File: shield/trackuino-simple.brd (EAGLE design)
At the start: 31.4 x 55.9 mm, 11 parts, among them T1 BC547, U1 ARDUINO_SHIELDNOHOLES

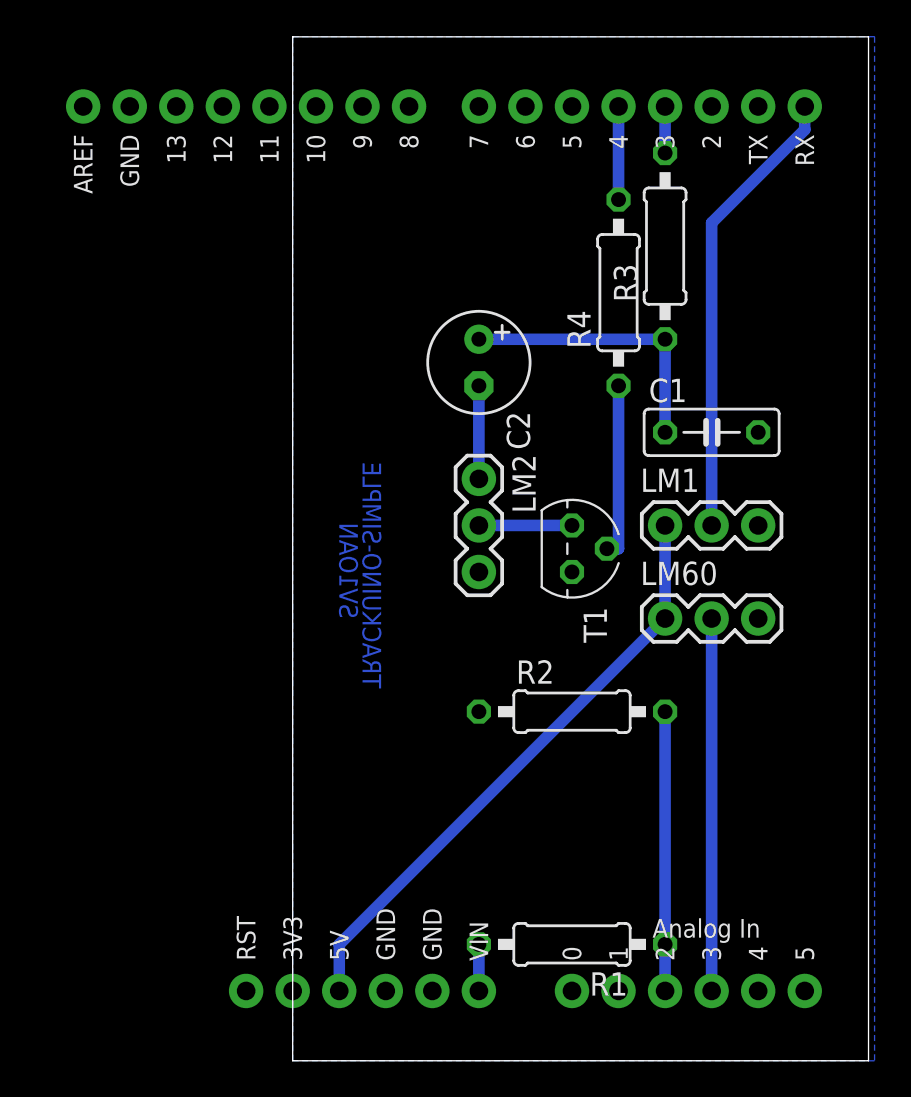
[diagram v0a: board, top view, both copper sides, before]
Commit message: Serial GPS support for shield
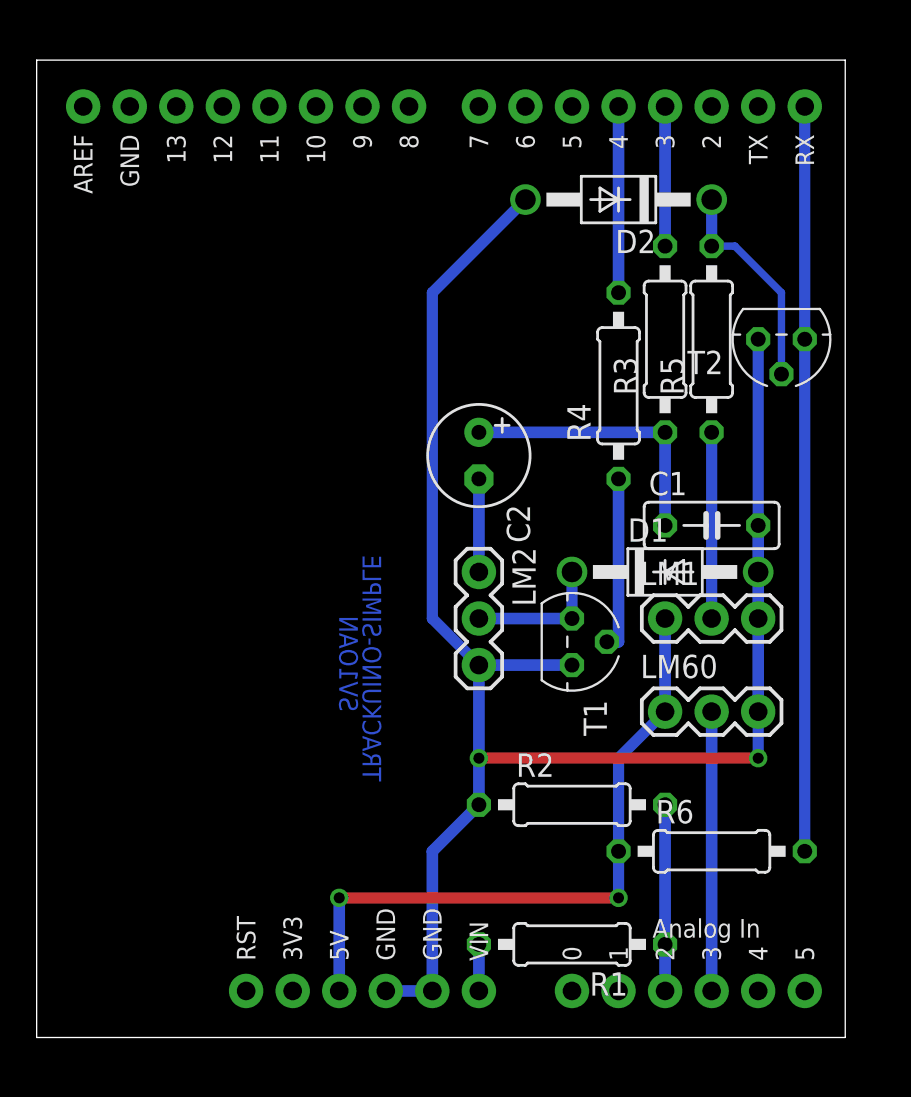
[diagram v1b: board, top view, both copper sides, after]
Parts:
- added D1, D2: (no value), diode:DO41-10
- added R5, R6: 10K, resistor:0207/10
- added T2: BC547, transistor:TO92
- moved LM1 5.08 mm to (44.5, 48.3)
- moved LM2 5.08 mm to (34.3, 50.8)
- moved R4 5.08 mm to (41.9, 61.0)
- moved C1 5.08 mm to (47.0, 53.3)
- moved C2 5.08 mm to (34.3, 57.1)
- moved LM60 5.08 mm to (44.5, 43.2)
- moved R2 5.08 mm to (39.4, 38.1)
- moved R3 5.08 mm to (44.5, 63.5)
- moved T1 5.08 mm to (39.4, 47.0)
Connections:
- new net N$10: LM1.2, R5.1
- new net N$5: D2.C, R5.2, T2.2
- net +5V: now also R6.1
- net GND: now also D1.A, D2.A, T2.1
- net N$1: now also R6.2, T2.3; no longer LM1.2
- net N$7: now also D1.C
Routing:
- net GND: track 0.00 -> 93.1 mm, vias 0 -> 2
- net N$1: track 25.0 -> 40.6 mm
- net N$5: track 0.00 -> 11.8 mm
- net N$10: track 0.00 -> 10.2 mm
- net N$6: track 2.54 -> 7.62 mm
- net N$3: track 5.08 -> 10.2 mm
- net N$2: track 20.3 -> 15.2 mm
- net A0: track 15.2 -> 10.2 mm
- net +5V: track 32.8 -> 36.6 mm, vias 0 -> 3
- net N$7: track 5.08 -> 7.62 mm
- removed copper zone on layer 16, net GND
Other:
- board size 31.4 x 55.9 mm -> 44.1 x 53.3 mm

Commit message: Change output filter capacitor value
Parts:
- C1: value 100nF -> 10nF
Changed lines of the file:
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@@
 <element name="LM2" library="SparkFun" package="1X03" value="" x="34.29" y="50.8" rot="R270"/>
 <element name="R3" library="rcl" package="0207/10" value="8K2" x="44.45" y="63.5" rot="R90"/>
-<element name="C1" library="resistor" package="C050-025X075" value="100nF" x="46.99" y="53.34"/>
+<element name="C1" library="resistor" package="C050-025X075" value="10nF" x="46.99" y="53.34"/>
 <element name="C2" library="resistor" package="E2,5-6" value="10uF" x="34.29" y="57.15" rot="R270"/>
 <element name="T2" library="transistor" package="TO92" value="BC547" x="50.8" y="63.5" rot="R180"/>
